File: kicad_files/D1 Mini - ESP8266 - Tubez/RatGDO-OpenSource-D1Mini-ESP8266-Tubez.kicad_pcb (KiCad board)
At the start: 2 copper layers, 51.8 x 65.8 mm, 35 parts, among them J1 Screw_Terminal_01x03, J2 Conn_01x11, J3 Screw_Terminal_01x02, Q1 2N7002, Q2 AO3400A, Q3 AO3400A, Q4 AO3400A, U1 WeMos_D1_mini, U2 K7805-500R3

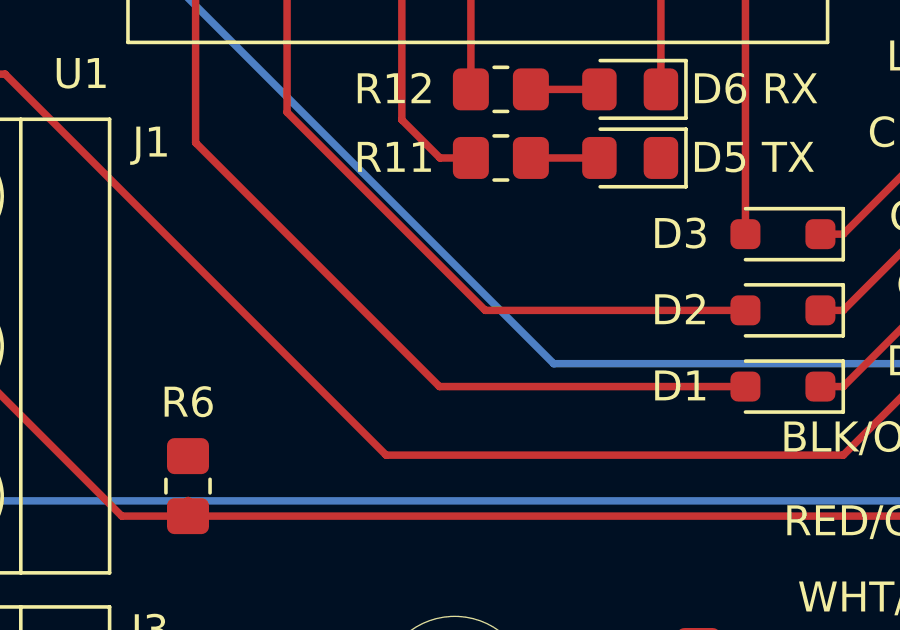
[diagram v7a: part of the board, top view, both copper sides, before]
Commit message: Add LED legend and move schematic onto grid
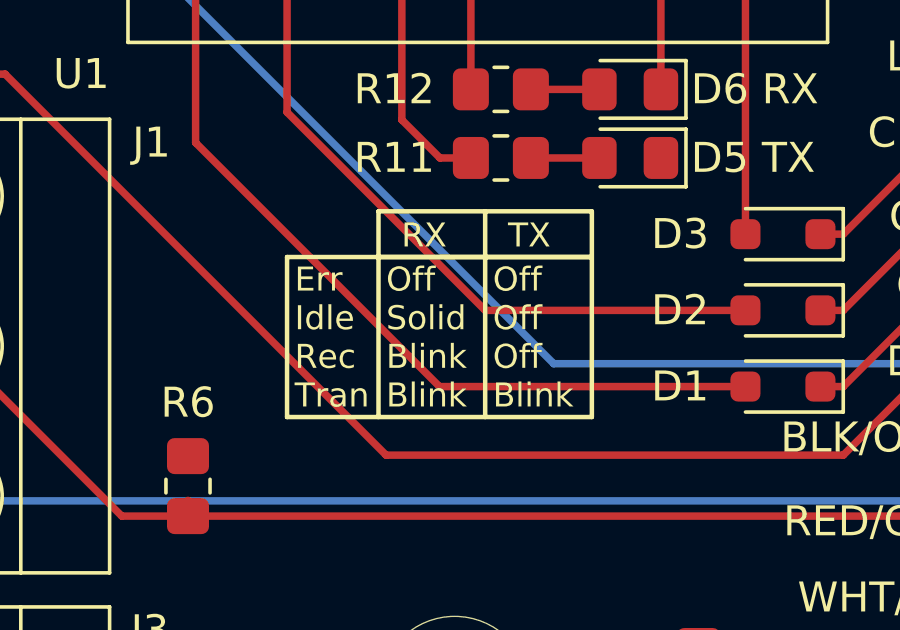
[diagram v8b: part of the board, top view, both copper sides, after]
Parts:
- G***: value LOGO -> Tubez_LOGO; footprint LOGO -> Custom Library:Tubez_LOGO
- J2: footprint Connector_PinHeader_2.54mm:PinHeader_1x11_P2.54mm_Vertical -> Custom Library:PinHeader_1x11_P2.54mm_Vertical_ExtendedPads
- JP1: footprint Jumper:SolderJumper-3_P1.3mm_Bridged2Bar12_RoundedPad1.0x1.5mm -> Custom Library:SolderJumper-3_P1.3mm_Bridged2Bar12_RoundedPad1.0x1.5mm_voltjump
- U2: footprint Converter_DCDC:Converter_DCDC_RECOM_R-78HB-0.5_THT -> Custom Library:Converter_DCDC_RECOM_R-78HB-0.5_THT_JLC_small
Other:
- board text added: "Err Idle Rec Tran"
- board text added: "Off Off Off Blink"
- board text added: "Off Solid Blink Blink"
